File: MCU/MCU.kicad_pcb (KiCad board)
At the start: 2 copper layers, 105.5 x 79 mm, 68 parts, among them J2 Conn_01x02, J3 Conn_01x02, J4 Conn_01x02, J5 Conn_01x02, U1 Nucleo_L432KC, U3 HHG1D-1, U4 AMC3302QDWERQ1, U5 HHG1D-1, U6 AMC3302QDWERQ1, U7 HHG1D-1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

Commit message: final?
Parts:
- added C28: 0.1uF, Capacitor_SMD:C_0201_0603Metric_Pad0.64x0.40mm_HandSolder, F.Cu at (173.1, 61.5)
- added C29: 0.1uF, Capacitor_SMD:C_0201_0603Metric_Pad0.64x0.40mm_HandSolder, F.Cu at (172.2, 61.5)
- added C30: 100nF, Capacitor_SMD:C_1206_3216Metric_Pad1.33x1.80mm_HandSolder, F.Cu at (178.4, 67.1)
- added J6: Conn_01x04, Connector_JST:JST_EH_B4B-EH-A_1x04_P2.50mm_Vertical, F.Cu at (164.9, 54.7)
- added R14: 400, Resistor_SMD:R_0603_1608Metric_Pad0.98x0.95mm_HandSolder, F.Cu at (178.2, 56.0)
- added R15: 25, Resistor_SMD:R_0201_0603Metric_Pad0.64x0.40mm_HandSolder, F.Cu at (170.3, 60.2)
- added R16: 25, Resistor_SMD:R_0201_0603Metric_Pad0.64x0.40mm_HandSolder, F.Cu at (172.5, 64.8)
- added R17: 25, Resistor_SMD:R_0201_0603Metric_Pad0.64x0.40mm_HandSolder, F.Cu at (175.3, 67.0)
- added R18: 25, Resistor_SMD:R_0201_0603Metric_Pad0.64x0.40mm_HandSolder, F.Cu at (176.0, 53.7)
- added U9: MAX31865xAP, Package_SO:SSOP-20_5.3x7.2mm_P0.65mm, F.Cu at (178.3, 61.8)
- moved TP2 9.16 mm to (165.4, 121.9)
- moved C15 0.20 mm to (140.6, 82.3)
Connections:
- R12 pad 1: /D11 -> /D4
- R13 pad 1: /D12 -> /D6
- U1 pad 12: unconnected-(U1-D9-Pad12) -> /D9
- U1 pad 13: unconnected-(U1-D10-Pad13) -> /D10
- U1 pad 16: unconnected-(U1-D13-Pad16) -> /D13
- U1 pad 7: unconnected-(U1-D4-Pad7) -> /D4
- U1 pad 9: unconnected-(U1-D6-Pad9) -> /D6
- U8 pad 14: /D12 -> /D6
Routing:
- net /D6: track 0.00 -> 50.7 mm, vias 0 -> 1
- net /D10: track 0.00 -> 49.8 mm
- net /D4: track 0.00 -> 30.5 mm, vias 0 -> 2
- net /D9: track 0.00 -> 26.6 mm, vias 0 -> 1
- net /D13: track 0.00 -> 23.4 mm, vias 0 -> 1
- net /D12: track 39.8 -> 20.5 mm
- net +3V3: track 93.7 -> 110.2 mm, vias 3 -> 4
- net Net-(U9-FORCE-): track 0.00 -> 15.5 mm
- net /RTD/RTDIN-: track 0.00 -> 13.4 mm, vias 0 -> 1
- net /RTD/RTDIN+: track 0.00 -> 12.1 mm, vias 0 -> 1
- net Net-(U9-ISENSOR): track 0.00 -> 9.49 mm
- net GND: track 22.8 -> 32.0 mm, vias 12 -> 17
- net Net-(U9-RTDIN-): track 0.00 -> 8.73 mm
- net Net-(R4-Pad2): track 15.8 -> 24.4 mm
- net Net-(U9-BIAS): track 0.00 -> 7.81 mm
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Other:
- board text added: "LED 1"
- board text added: "LED 2"
- board text added: "LED 3"
- board text added: "LED1 Test"
- board text added: "LED1 Test MCU CTRL"
- board text added: "LED2 Test"
- board text added: "LED2 Test MCU CTRL"
- board text added: "LED3 Test"
- board text added: "LED3 Test MCU CTRL"
- board text added: "PS"
- board text added: "RTD"

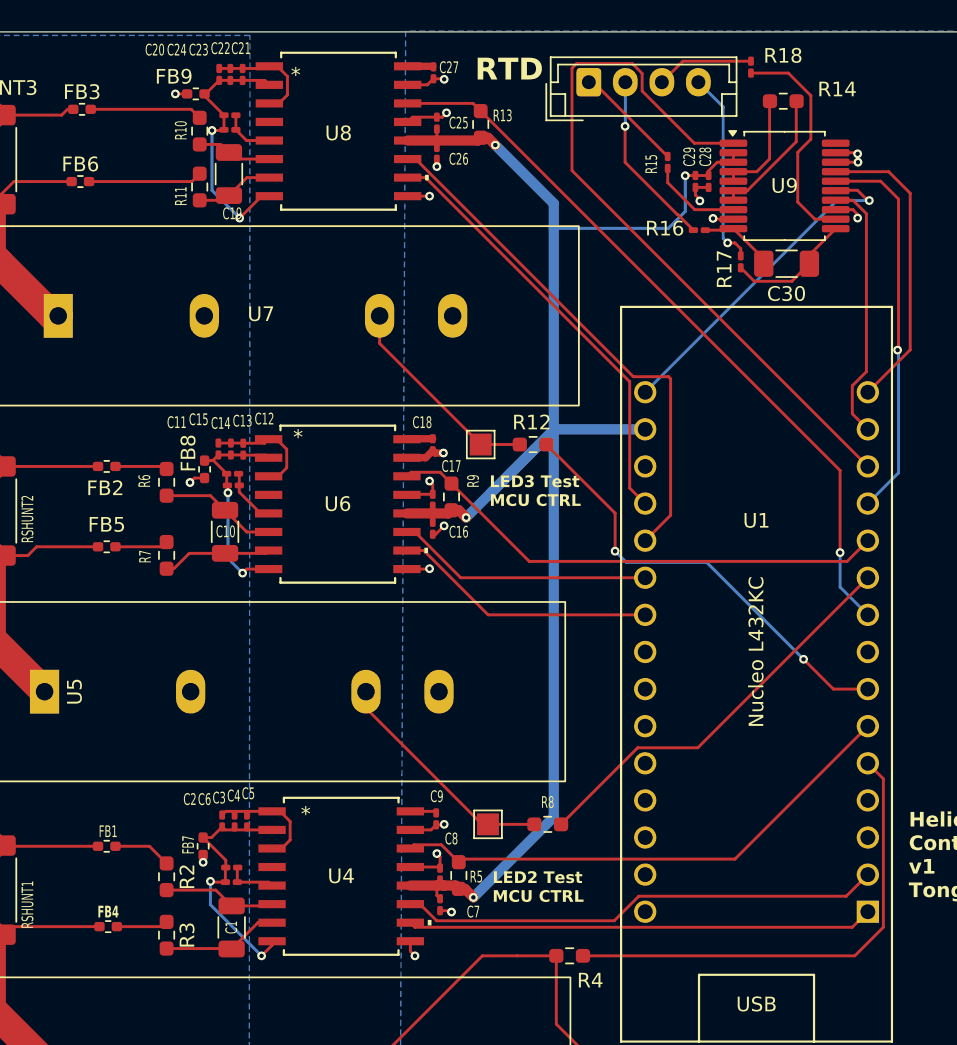
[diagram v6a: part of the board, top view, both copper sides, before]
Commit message: layout fixes
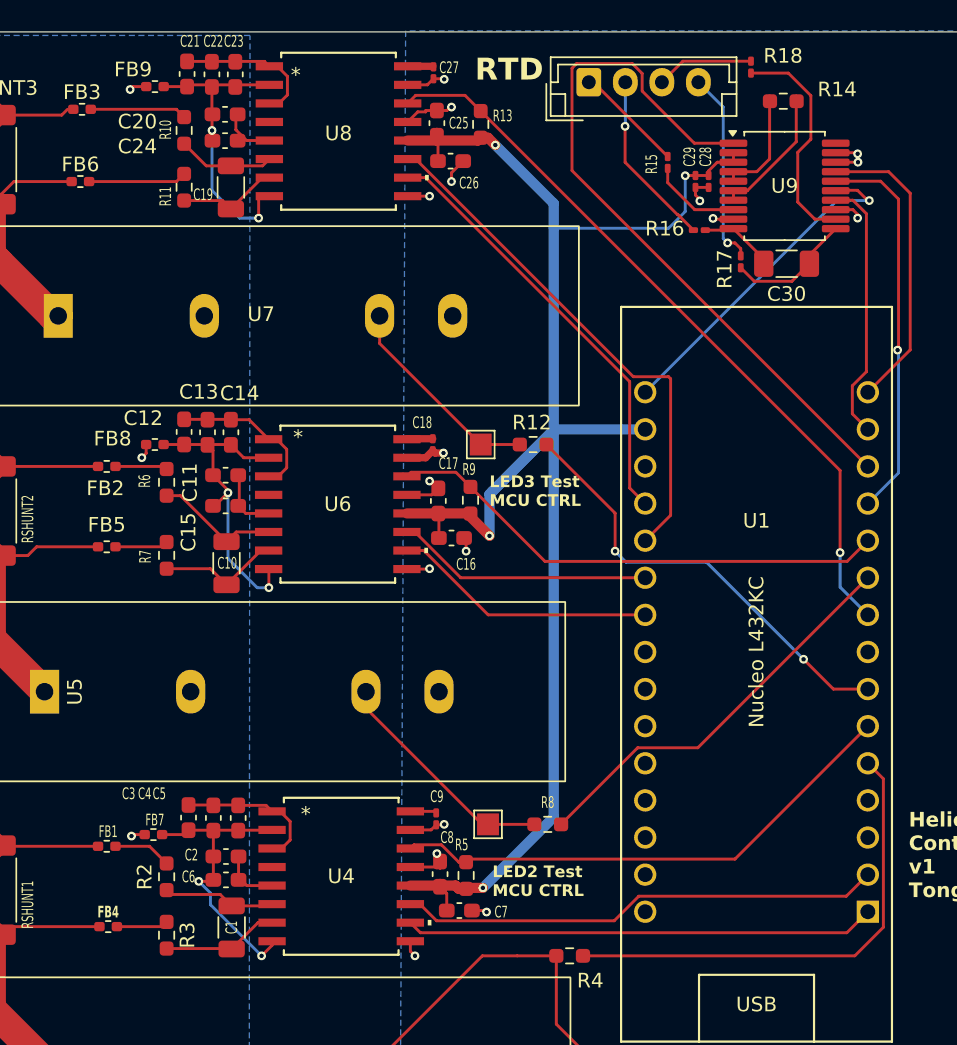
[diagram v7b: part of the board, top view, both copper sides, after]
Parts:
- C11, C12, C13, C14, C15, C16, C17, C2, C20, C21, C22, C23, C24, C25, C26, C3, C4, C5, C6, C7, C8: footprint Capacitor_SMD:C_0201_0603Metric_Pad0.64x0.40mm_HandSolder -> Capacitor_SMD:C_0603_1608Metric_Pad1.08x0.95mm_HandSolder
- moved FB8 3.80 mm to (135.2, 79.5), turned to 0 degrees
- moved FB7 3.50 mm to (135.1, 106.2), turned to 0 degrees
- moved FB9 2.84 mm to (135.2, 55.0)
- moved C12 2.62 mm to (137.2, 78.6)
- moved C3 2.31 mm to (137.5, 105.0)
- moved C21 2.20 mm to (137.4, 54.1)
- moved C10 2.15 mm to (140.1, 87.6)
- moved C13 1.97 mm to (138.8, 78.7)
- moved C15 1.50 mm to (140.0, 83.7)
- moved C4 1.47 mm to (139.2, 105.1)
- moved C16 1.45 mm to (155.5, 85.9), turned to 0 degrees
- moved C14 1.43 mm to (140.4, 78.7)
- moved C7 1.38 mm to (156.0, 111.4), turned to 0 degrees
- moved R9 1.32 mm to (156.8, 83.3)
- moved C22 1.26 mm to (139.1, 54.2)
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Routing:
- net Net-(U6-DCDC_HGND): track 15.8 -> 22.9 mm
- net +3V3: track 110.2 -> 116.2 mm
- net Net-(U8-INP): track 3.77 -> 6.65 mm
- net GND: track 32.0 -> 34.8 mm
- net Net-(U6-DCDC_OUT): track 7.83 -> 10.6 mm
- net Net-(U4-DCDC_HGND): track 17.8 -> 20.2 mm
- net Net-(U4-DCDC_OUT): track 7.79 -> 10.2 mm
- net Net-(U8-DCDC_OUT): track 7.77 -> 10.0 mm
- net Net-(U8-DCDC_HGND): track 18.2 -> 20.5 mm
- net Net-(U8-INN): track 4.95 -> 6.96 mm
- net Net-(FB3-Pad2): track 7.70 -> 6.61 mm
- net Net-(FB6-Pad2): track 7.79 -> 6.72 mm
- net Net-(U6-INN): track 7.50 -> 8.41 mm
- net GND1: track 2.43 -> 3.16 mm
- net Net-(U6-HLDO_OUT): track 3.89 -> 4.49 mm
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
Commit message: final changes
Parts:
- C18, C27, C28, C29, C9: footprint Capacitor_SMD:C_0201_0603Metric_Pad0.64x0.40mm_HandSolder -> Capacitor_SMD:C_0603_1608Metric_Pad1.08x0.95mm_HandSolder
- FB1, FB2, FB3, FB4, FB5, FB6, FB7, FB8, FB9: footprint Resistor_SMD:R_0402_1005Metric_Pad0.72x0.64mm_HandSolder -> Resistor_SMD:R_0603_1608Metric_Pad0.98x0.95mm_HandSolder
- R15, R16, R17, R18: footprint Resistor_SMD:R_0201_0603Metric_Pad0.64x0.40mm_HandSolder -> Resistor_SMD:R_0603_1608Metric_Pad0.98x0.95mm_HandSolder
- moved R15 2.13 mm to (168.3, 59.5)
- moved R18 1.45 mm to (177.4, 53.3), turned to 180 degrees
- moved FB7 1.43 mm to (134.8, 104.8)
- moved C29 1.40 mm to (170.8, 61.6)
- moved R17 1.20 mm to (174.5, 67.9)
- moved R16 1.19 mm to (171.3, 65.0)
- moved FB9 0.66 mm to (134.6, 54.9)
- moved FB8 0.60 mm to (134.6, 79.5)
- moved C28 0.52 mm to (172.6, 61.6)
- moved C18 0.48 mm to (154.7, 79.5)
- moved C9 0.48 mm to (154.9, 105.0)
- moved C27 0.47 mm to (154.7, 53.9)
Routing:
- net Net-(U9-FORCE+): track 6.24 -> 26.4 mm, vias 0 -> 2
- net GND: track 34.8 -> 38.8 mm
- net /RTD/FORCE+: track 7.51 -> 5.45 mm
- net Net-(U9-FORCE-): track 15.5 -> 13.8 mm
- net Net-(U9-RTDIN+): track 5.23 -> 5.97 mm
- net Net-(U8-DCDC_IN): track 1.73 -> 2.45 mm
- net Net-(U6-DCDC_IN): track 1.78 -> 2.45 mm
- net Net-(U4-DCDC_IN): track 1.81 -> 2.43 mm
- net Net-(U9-RTDIN-): track 8.73 -> 9.34 mm
